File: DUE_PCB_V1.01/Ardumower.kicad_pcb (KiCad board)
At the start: 2 copper layers, 169.4 x 95.5 mm, 77 parts, among them J1 I2C_1, J10 P_Left, J11 P_Right, J12 Sonar_R, J13 Sonar_C, J14 Sonar_L, J15 Bumper, J16 Button, J17 Button, J18 Button, J19 Button, J2 I2C_2, J20 5V IN, J21 Remote, J22 PCB_2, J23 5V, J24 3.3V IN, J25 3.3V, J26 GND, J27 RX & TX, J28 Motor Left, J29 Cutter Motor, J3 I2C_3, J30 Motor Right, J4 DS3231 RTC, J5 9V IN, J6 Drop_Left, J7 Drop_Right, J8 Tilt, J9 Rain, U1 MC33926, U2 MC33926

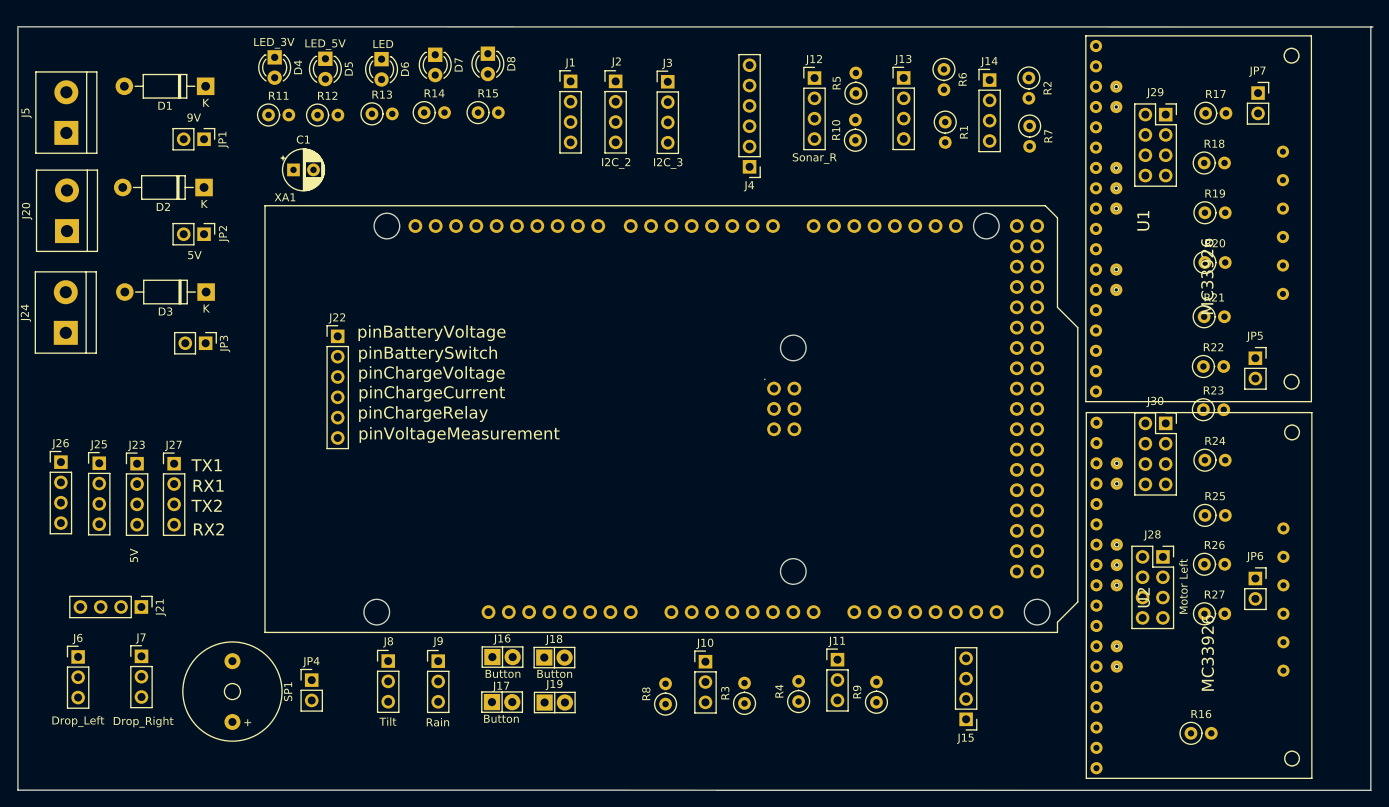
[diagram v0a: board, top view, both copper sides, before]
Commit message: Add Power Connector for 5V and 3.3V
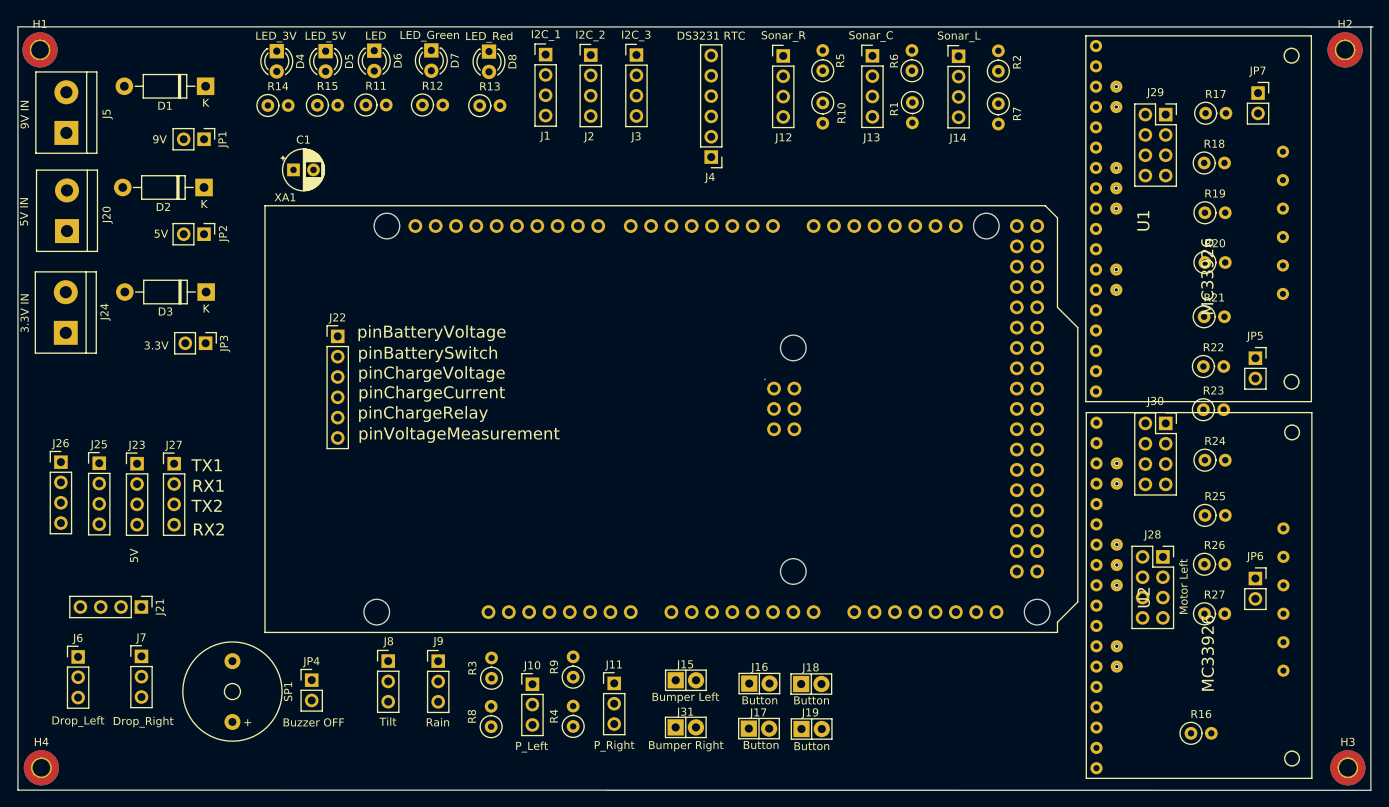
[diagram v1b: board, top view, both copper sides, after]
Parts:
- added H1: MountingHole_Pad, MountingHole:MountingHole_2.2mm_M2_Pad_TopBottom, F.Cu at (42.0, 38.4)
- added H2: MountingHole_Pad, MountingHole:MountingHole_2.2mm_M2_Pad_TopBottom, F.Cu at (205.1, 38.4)
- added H3: MountingHole_Pad, MountingHole:MountingHole_2.2mm_M2_Pad_TopBottom, F.Cu at (205.5, 128.1)
- added H4: MountingHole_Pad, MountingHole:MountingHole_2.2mm_M2_Pad_TopBottom, F.Cu at (42.2, 128.1)
- added J31: Bumper Right, Zimprich:Pin_Header_KK110_1x02_3D, F.Cu at (122.7, 123.1)
- J15: value Bumper -> Bumper Left; footprint Connector_PinHeader_2.54mm:PinHeader_1x04_P2.54mm_Vertical -> Zimprich:Pin_Header_KK110_1x02_3D
- moved R9 38.0 mm to (108.6, 116.8)
- moved J15 35.4 mm to (122.7, 117.2), turned to 0 degrees
- moved J17 32.3 mm to (131.9, 123.2)
- moved J16 32.3 mm to (131.9, 117.6)
- moved J18 32.3 mm to (138.4, 117.7)
- moved J19 32.3 mm to (138.4, 123.3)
- moved R3 31.8 mm to (98.4, 116.9)
- moved R4 28.4 mm to (108.6, 123.0)
- moved J11 28.1 mm to (113.8, 117.6)
- moved R8 22.0 mm to (98.4, 123.0)
- moved J10 21.8 mm to (103.5, 117.7)
- moved R15 20.1 mm to (76.7, 45.3)
- moved R14 19.6 mm to (70.5, 45.3)
- moved R13 13.5 mm to (97.0, 45.4)
- moved R12 13.2 mm to (89.8, 45.3)
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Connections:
- J15 pad 2: pinBumperRight -> pinBumperLeft

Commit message: Design changes
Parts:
- J17: value Button -> US1
- J18, J19: value Button -> US3
- moved J6 98.8 mm to (145.5, 117.6)
- moved J7 96.6 mm to (151.3, 117.6)
- moved J21 75.0 mm to (106.5, 53.8)
- moved R17 73.7 mm to (187.5, 120.0)
- moved R18 61.4 mm to (187.5, 113.9)
- moved JP7 49.7 mm to (193.7, 93.5)
- moved R19 49.0 mm to (187.6, 107.7)
- moved J22 43.9 mm to (42.8, 98.7)
- moved JP5 40.5 mm to (193.5, 117.4)
- moved JP6 34.2 mm to (194.0, 70.3)
- moved R27 25.9 mm to (187.9, 83.0)
- moved J29 20.2 mm to (182.2, 66.7)
- moved R26 13.5 mm to (187.8, 89.2)
- moved J28 12.2 mm to (182.4, 114.0)
- moved R24 11.7 mm to (187.7, 101.4)
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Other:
- board size 169.4 x 95.5 mm -> 169.2 x 95.5 mm

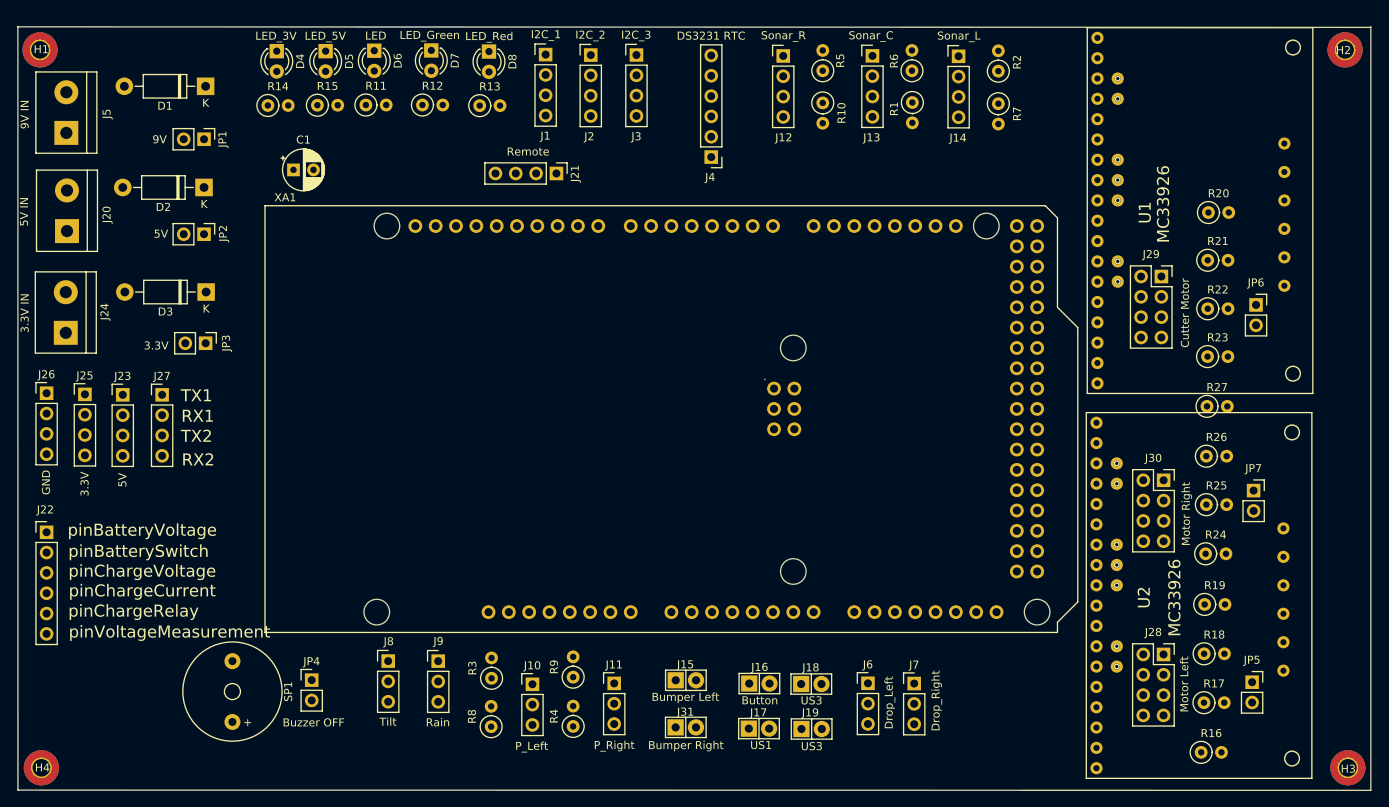
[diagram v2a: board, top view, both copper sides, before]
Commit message: first test
JP2 and JP3 redraw
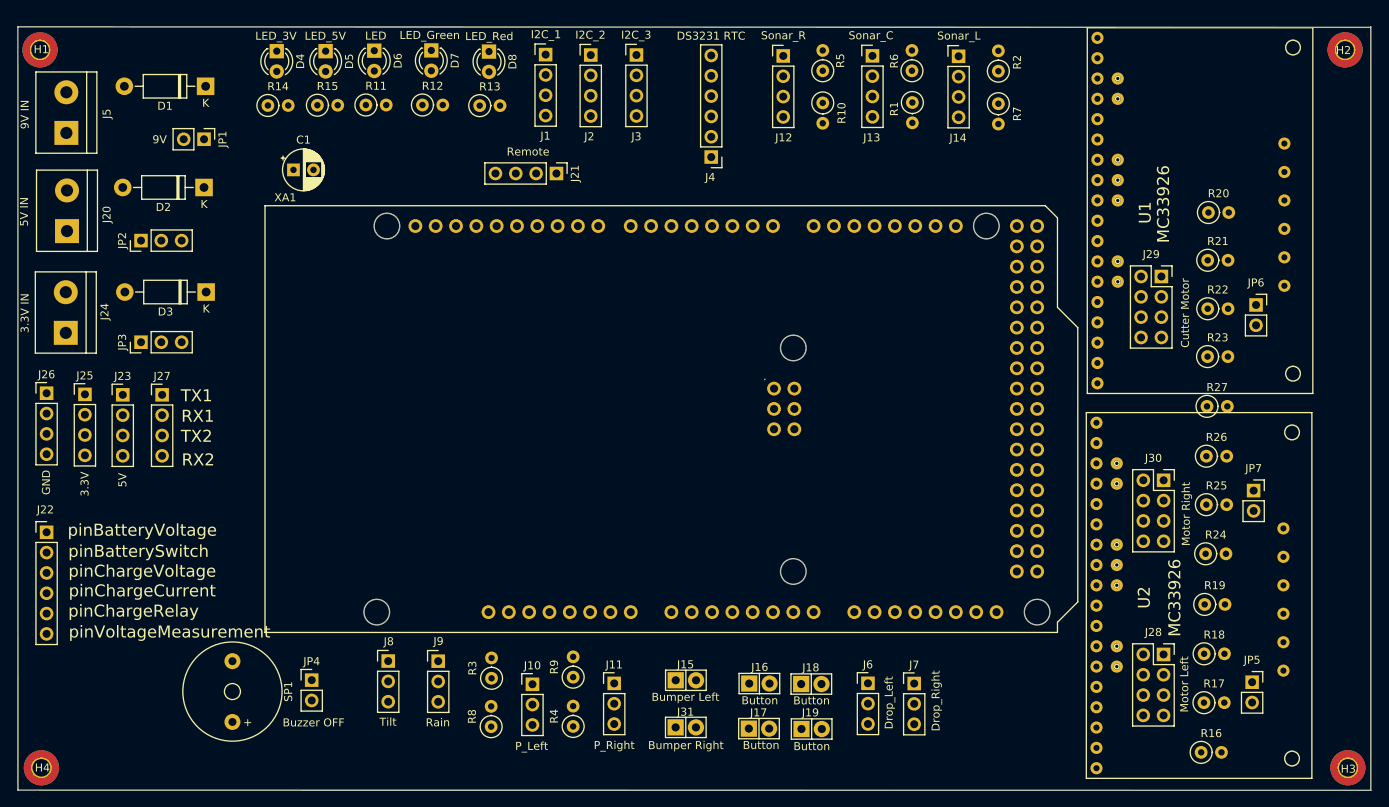
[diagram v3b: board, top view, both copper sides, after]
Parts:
- J17: value US1 -> Button
- J18, J19: value US3 -> Button
- JP2: value 5V -> Sel 5V; footprint Connector_PinHeader_2.54mm:PinHeader_1x02_P2.54mm_Vertical -> Connector_PinHeader_2.54mm:PinHeader_1x03_P2.54mm_Vertical
- JP3: value 3.3V -> Sel 3.3V; footprint Connector_PinHeader_2.54mm:PinHeader_1x02_P2.54mm_Vertical -> Connector_PinHeader_2.54mm:PinHeader_1x03_P2.54mm_Vertical
- moved JP3 8.08 mm to (54.6, 74.9), turned to 90 degrees
- moved JP2 7.92 mm to (54.6, 62.2), turned to 90 degrees
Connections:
- J29 pad 5: (no net) -> MotorMowBreak
- J4 pad 1: (no net) -> Net-(J4-Pad1)
- J4 pad 2: (no net) -> Net-(J4-Pad2)
- U1 pad 1: (no net) -> Net-(U1-Pad1)
- U1 pad 11: (no net) -> Net-(U1-Pad11)
- U1 pad 12: (no net) -> Net-(U1-Pad12)
- U1 pad 19: (no net) -> Net-(U1-Pad19)
- U1 pad 20: (no net) -> Net-(U1-Pad20)
- U1 pad 23: (no net) -> Net-(U1-Pad23)
- U1 pad 24: (no net) -> Net-(U1-Pad24)
- U2 pad 1: (no net) -> Net-(U2-Pad1)
- U2 pad 11: (no net) -> Net-(U2-Pad11)
- U2 pad 12: (no net) -> Net-(U2-Pad12)
- U2 pad 19: (no net) -> Net-(U2-Pad19)
- U2 pad 20: (no net) -> Net-(U2-Pad20)
- U2 pad 23: (no net) -> Net-(U2-Pad23)
- U2 pad 24: (no net) -> Net-(U2-Pad24)
- XA1 pad 3V3: (no net) -> +3V3
- XA1 pad 5V1: (no net) -> +5V
- XA1 pad 5V2: (no net) -> Net-(XA1-Pad5V2)
- XA1 pad 5V3: (no net) -> Net-(XA1-Pad5V3)
- XA1 pad 5V4: (no net) -> Net-(XA1-Pad5V4)
- XA1 pad A10: (no net) -> Net-(XA1-PadA10)
- XA1 pad A6: (no net) -> pinPerimeterCenter
- XA1 pad CANT: (no net) -> pinOdometryRight2
- XA1 pad D0: (no net) -> RX0
- XA1 pad D1: (no net) -> TX0
- XA1 pad D14: (no net) -> GPS_RX
- XA1 pad D15: (no net) -> GPS_TX
- XA1 pad D40: (no net) -> pinLawnFrontRecv
- XA1 pad D41: (no net) -> pinLawnFrontSend
- XA1 pad D42: (no net) -> pinLawnBackRecv
- XA1 pad D43: (no net) -> pinLawnBackSend
- XA1 pad D49: (no net) -> Net-(XA1-PadD49)
- XA1 pad D8: (no net) -> Net-(XA1-PadD8)
- XA1 pad D9: (no net) -> Net-(XA1-PadD9)
- XA1 pad DAC1: (no net) -> pinOdometryLeft2
- XA1 pad GND4: (no net) -> Net-(XA1-PadGND4)
- XA1 pad MISO: (no net) -> Net-(XA1-PadMISO)
- XA1 pad MOSI: (no net) -> Net-(XA1-PadMOSI)
- XA1 pad RST1: (no net) -> Reset
- XA1 pad RST2: (no net) -> Net-(XA1-PadRST2)
- XA1 pad SCK: (no net) -> Net-(XA1-PadSCK)

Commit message: test
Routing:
- net GND: track 0.00 -> 183.1 mm
- net pinMotorMowSense: track 0.00 -> 92.6 mm
- net Net-(D2-Pad1): track 0.00 -> 12.1 mm
- net Net-(D1-Pad2): track 0.00 -> 7.56 mm
- net Net-(D3-Pad2): track 0.00 -> 7.39 mm
- net Net-(D2-Pad2): track 0.00 -> 7.12 mm
- net Net-(D1-Pad1): track 0.00 -> 6.70 mm
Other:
- net class Power added: clearance 0.2, trace_width 1, via_dia 0.8, via_drill 0.4
